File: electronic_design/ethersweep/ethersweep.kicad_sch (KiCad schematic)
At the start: 97 parts, among them J1 AVR-ISP-6, J10 HR911105A, J11 Conn_01x04_Male, J2 Conn_01x02_Male, J3 Conn_01x04_Female, J4 Conn_01x02_Male, J5 Conn_01x02_Male, J6 Conn_01x07_Female, J7 Conn_01x07_Male, J8 AVR-ISP-6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

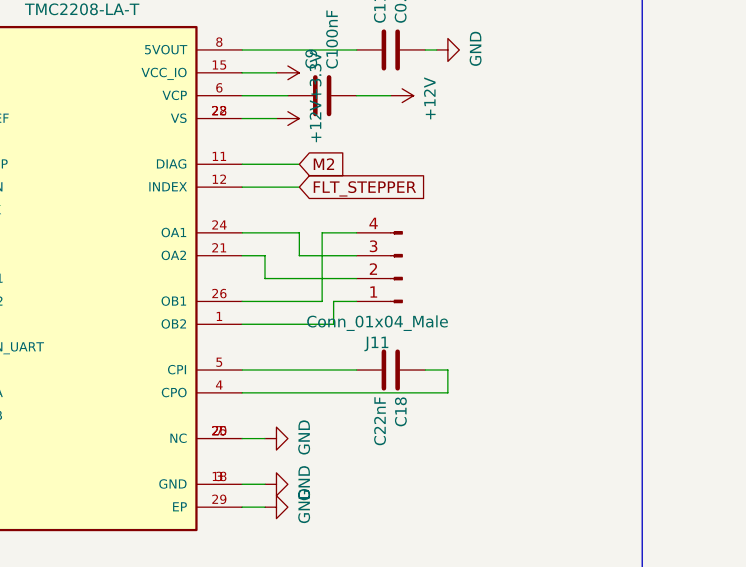
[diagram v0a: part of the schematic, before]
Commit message: changed pinout for nema17 motor to be parallel to connector
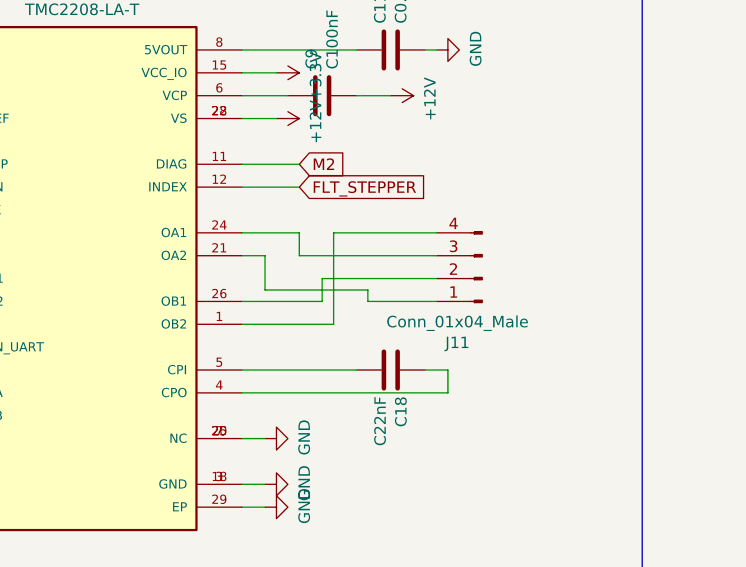
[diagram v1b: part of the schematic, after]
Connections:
- net at U3.1 (OB2): now also J11.4 (Pin_4); no longer J11.1 (Pin_1)
- net at U3.21 (OA2): now also J11.1 (Pin_1); no longer J11.2 (Pin_2)
- net at U3.26 (OB1): now also J11.2 (Pin_2); no longer J11.4 (Pin_4)
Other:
- moved on the sheet: J11
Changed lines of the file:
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@@
     (stroke (width 0) (type default) (color 0 0 0 0))
   )
+  (wire (pts (xy 365.76 180.34) (xy 377.19 180.34))
+    (stroke (width 0) (type default) (color 0 0 0 0))
+  )
   (wire (pts (xy 111.76 237.49) (xy 105.41 237.49))
     (stroke (width 0) (type default) (color 0 0 0 0))
@@
     (stroke (width 0) (type default) (color 0 0 0 0))
   )
-  (wire (pts (xy 358.14 185.42) (xy 368.3 185.42))
-    (stroke (width 0) (type default) (color 0 0 0 0))
-  )
   (wire (pts (xy 162.56 90.17) (xy 167.64 90.17))
     (stroke (width 0) (type default) (color 0 0 0 0))
@@
     (stroke (width 0) (type default) (color 0 0 0 0))
   )
+  (wire (pts (xy 369.57 186.69) (xy 369.57 187.96))
+    (stroke (width 0) (type default) (color 0 0 0 0))
+  )
   (wire (pts (xy 189.23 127) (xy 189.23 121.92))
     (stroke (width 0) (type default) (color 0 0 0 0))
@@
     (stroke (width 0) (type default) (color 0 0 0 0))
   )
+  (wire (pts (xy 369.57 187.96) (xy 377.19 187.96))
+    (stroke (width 0) (type default) (color 0 0 0 0))
+  )
   (wire (pts (xy 214.63 179.07) (xy 222.25 179.07))
     (stroke (width 0) (type default) (color 0 0 0 0))
@@
     (stroke (width 0) (type default) (color 0 0 0 0))
   )
-  (wire (pts (xy 364.49 180.34) (xy 364.49 187.96))
-    (stroke (width 0) (type default) (color 0 0 0 0))
-  )
   (wire (pts (xy 171.45 121.92) (xy 171.45 128.27))
     (stroke (width 0) (type default) (color 0 0 0 0))
@@
     (stroke (width 0) (type default) (color 0 0 0 0))
   )
+  (wire (pts (xy 358.14 186.69) (xy 369.57 186.69))
+    (stroke (width 0) (type default) (color 0 0 0 0))
+  )
   (wire (pts (xy 140.97 190.5) (xy 140.97 204.47))
     (stroke (width 0) (type default) (color 0 0 0 0))
@@
     (stroke (width 0) (type default) (color 0 0 0 0))
   )
+  (wire (pts (xy 365.76 180.34) (xy 365.76 190.5))
+    (stroke (width 0) (type default) (color 0 0 0 0))
+  )
   (wire (pts (xy 364.49 187.96) (xy 355.6 187.96))
     (stroke (width 0) (type default) (color 0 0 0 0))
@@
     (stroke (width 0) (type default) (color 0 0 0 0))
   )
-  (wire (pts (xy 364.49 180.34) (xy 368.3 180.34))
+  (wire (pts (xy 364.49 185.42) (xy 364.49 187.96))
     (stroke (width 0) (type default) (color 0 0 0 0))
   )
@@
     (stroke (width 0) (type default) (color 0 0 0 0))
   )
-  (wire (pts (xy 358.14 182.88) (xy 358.14 185.42))
-    (stroke (width 0) (type default) (color 0 0 0 0))
-  )
   (polyline (pts (xy 285.75 146.05) (xy 400.05 146.05))
     (stroke (width 0) (type default) (color 0 0 0 0))
@@
     (stroke (width 0) (type default) (color 0 0 0 0))
   )
-  (wire (pts (xy 365.76 187.96) (xy 365.76 190.5))
-    (stroke (width 0) (type default) (color 0 0 0 0))
-  )
   (wire (pts (xy 184.15 87.63) (xy 184.15 92.71))
     (stroke (width 0) (type default) (color 0 0 0 0))
@@
     (stroke (width 0) (type default) (color 0 0 0 0))
   )
-  (wire (pts (xy 368.3 187.96) (xy 365.76 187.96))
-    (stroke (width 0) (type default) (color 0 0 0 0))
-  )
   (wire (pts (xy 355.6 198.12) (xy 378.46 198.12))
     (stroke (width 0) (type default) (color 0 0 0 0))
@@
     (stroke (width 0) (type default) (color 0 0 0 0))
   )
+  (wire (pts (xy 358.14 182.88) (xy 358.14 186.69))
+    (stroke (width 0) (type default) (color 0 0 0 0))
+  )
   (wire (pts (xy 219.71 35.56) (xy 218.44 35.56))
     (stroke (width 0) (type default) (color 0 0 0 0))
@@
     (stroke (width 0) (type default) (color 0 0 0 0))
   )
-  (wire (pts (xy 361.95 182.88) (xy 368.3 182.88))
+  (wire (pts (xy 361.95 182.88) (xy 377.19 182.88))
     (stroke (width 0) (type default) (color 0 0 0 0))
   )
@@
     (stroke (width 0) (type default) (color 0 0 0 0))
   )
+  (wire (pts (xy 364.49 185.42) (xy 377.19 185.42))
+    (stroke (width 0) (type default) (color 0 0 0 0))
+  )
   (wire (pts (xy 46.99 234.95) (xy 46.99 237.49))
     (stroke (width 0) (type default) (color 0 0 0 0))
@@
     (pin "2")
   )
-  (symbol (lib_id "Connector:Conn_01x04_Male") (at 373.38 185.42 180) (unit 1)
+  (symbol (lib_id "Connector:Conn_01x04_Male") (at 382.27 185.42 180) (unit 1)
     (in_bom yes) (on_board yes)
-    (property "Reference" "J11" (id 0) (at 370.6368 192.5574 0))
-    (property "Value" "Conn_01x04_Male" (id 1) (at 370.6368 190.246 0))
-    (property "Footprint" "Connector_JST:JST_EH_S4B-EH_1x04_P2.50mm_Horizontal" (id 2) (at 373.38 185.42 0)
+    (property "Reference" "J11" (id 0) (at 379.5268 192.5574 0))
+    (property "Value" "Conn_01x04_Male" (id 1) (at 379.5268 190.246 0))
+    (property "Footprint" "Connector_JST:JST_EH_S4B-EH_1x04_P2.50mm_Horizontal" (id 2) (at 382.27 185.42 0)
       (effects (font (size 1.27 1.27)) hide)
     )
-    (property "Datasheet" "~" (id 3) (at 373.38 185.42 0)
+    (property "Datasheet" "~" (id 3) (at 382.27 185.42 0)
       (effects (font (size 1.27 1.27)) hide)
     )
